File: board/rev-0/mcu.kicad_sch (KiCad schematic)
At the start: 53 parts, among them J1 I2C, J2 Conn_01x08, J3 USB_C_Receptacle_USB2.0_16P, J4 Conn_01x03, J5 Conn_01x03, J6 Conn_01x03, J7 Conn_01x03, U1 ESP32-S3-WROOM-1, U7 SN74LV1T34DBV

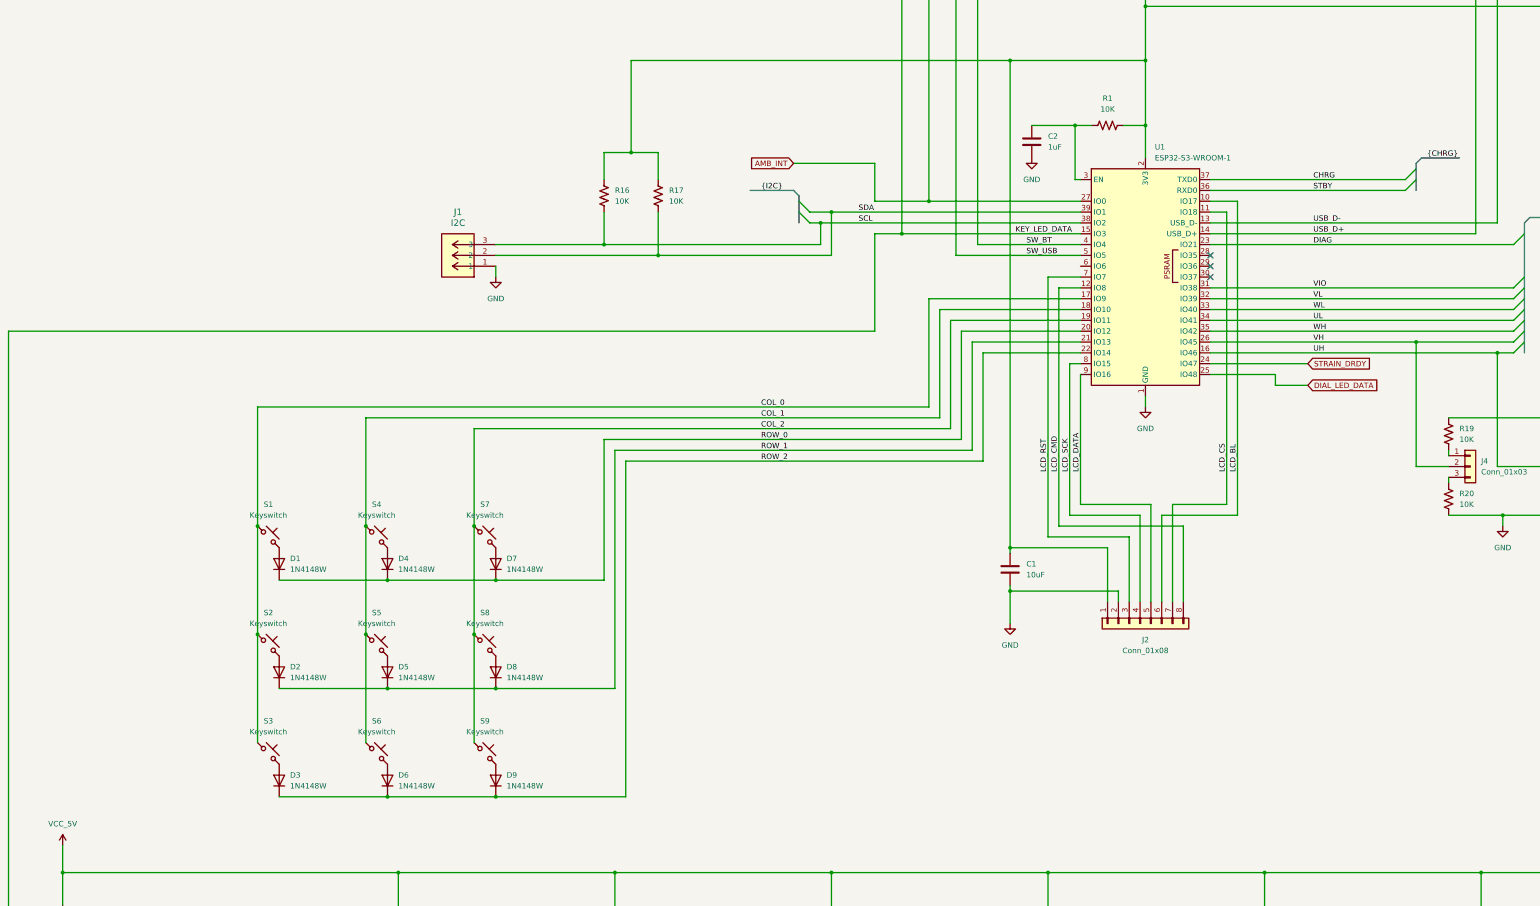
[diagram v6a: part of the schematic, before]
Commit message: Added power circuitry
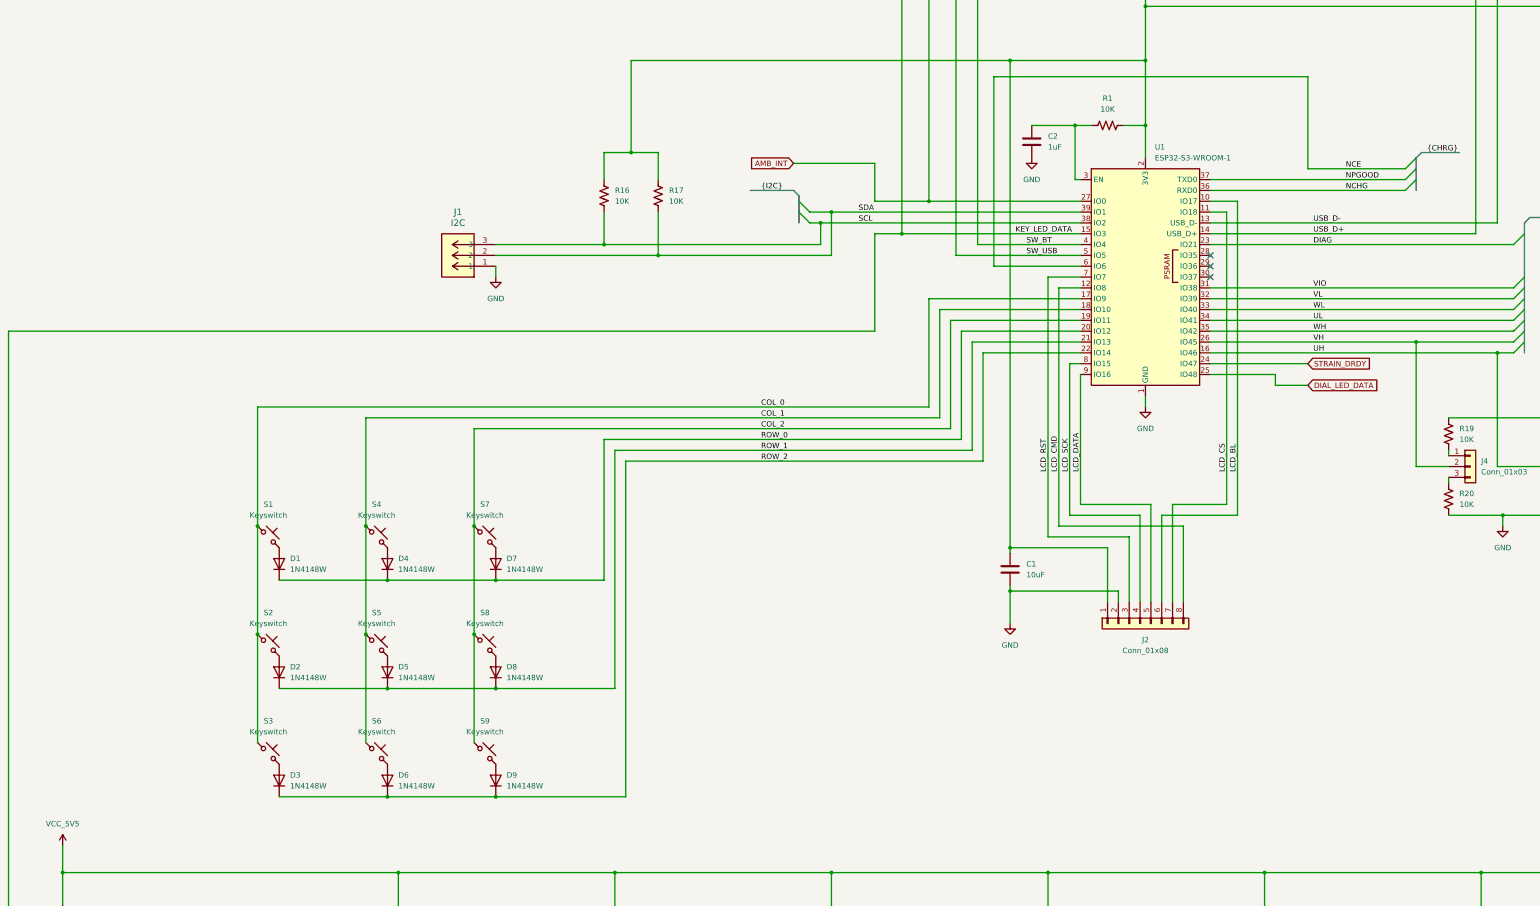
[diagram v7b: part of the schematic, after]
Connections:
- net NCE: now reaches U1.6 (IO6)
- net CHRG renamed NPGOOD
- net STBY renamed NCHG
- net VCC_5V renamed VCC_5V5
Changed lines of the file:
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@@
 	(title_block
 		(title "MCU")
-		(date "2025-03-28")
+		(date "2025-04-20")
 		(rev "0")
 		(company "Biro")
@@
 	)
 	(bus_alias "CHRG"
-		(members "CHRG" "STBY")
+		(members "NPGOOD" "NCHG" "NCE")
 	)
 	(junction
@@
 	)
 	(bus_entry
+		(at 368.3 177.8)
+		(size -2.54 2.54)
+		(stroke
+			(width 0)
+			(type default)
+		)
+	)
+	(bus_entry
 		(at 223.52 185.42)
 		(size 2.54 2.54)
@@
 	)
 	(bus_entry
-		(at 368.3 177.8)
+		(at 393.7 213.36)
 		(size -2.54 2.54)
 		(stroke
@@
 	)
 	(bus_entry
-		(at 393.7 213.36)
+		(at 368.3 175.26)
 		(size -2.54 2.54)
 		(stroke
@@
 	(wire
 		(pts
+			(xy 342.9 156.21) (xy 269.24 156.21)
+		)
+		(stroke
+			(width 0)
+			(type default)
+		)
+	)
+	(wire
+		(pts
 			(xy 311.15 256.54) (xy 311.15 279.4)
 		)
@@
 		)
 	)
+	(bus
+		(pts
+			(xy 368.3 177.8) (xy 368.3 175.26)
+		)
+		(stroke
+			(width 0)
+			(type default)
+		)
+	)
 	(wire
 		(pts
@@
 		)
 	)
-	(bus
-		(pts
-			(xy 368.3 176.53) (xy 368.3 177.8)
-		)
-		(stroke
-			(width 0)
-			(type default)
-		)
-	)
 	(wire
 		(pts
@@
 		)
 	)
+	(wire
+		(pts
+			(xy 365.76 177.8) (xy 342.9 177.8)
+		)
+		(stroke
+			(width 0)
+			(type default)
+		)
+	)
 	(bus
 		(pts
@@
 	(wire
 		(pts
-			(xy 320.04 182.88) (xy 365.76 182.88)
-		)
-		(stroke
-			(width 0)
-			(type default)
-		)
-	)
-	(wire
-		(pts
 			(xy 320.04 205.74) (xy 391.16 205.74)
 		)
@@
 		)
 	)
-	(bus
-		(pts
-			(xy 369.57 175.26) (xy 378.46 175.26)
-		)
-		(stroke
-			(width 0)
-			(type default)
-		)
-	)
 	(wire
 		(pts
@@
 		)
 	)
-	(wire
+	(bus
 		(pts
-			(xy 320.04 180.34) (xy 365.76 180.34)
+			(xy 369.57 173.99) (xy 378.46 173.99)
 		)
 		(stroke
@@
 	(wire
 		(pts
+			(xy 342.9 177.8) (xy 342.9 156.21)
+		)
+		(stroke
+			(width 0)
+			(type default)
+		)
+	)
+	(wire
+		(pts
 			(xy 231.14 342.9) (xy 231.14 358.14)
 		)
@@
 		)
 	)
+	(bus
+		(pts
+			(xy 368.3 182.88) (xy 368.3 180.34)
+		)
+		(stroke
+			(width 0)
+			(type default)
+		)
+	)
 	(wire
 		(pts
@@
 		)
 	)
-	(bus
+	(wire
 		(pts
-			(xy 393.7 205.74) (xy 393.7 208.28)
+			(xy 269.24 156.21) (xy 269.24 200.66)
 		)
 		(stroke
@@
 		)
 	)
-	(wire
+	(bus
 		(pts
-			(xy 262.89 92.71) (xy 270.51 92.71)
+			(xy 393.7 205.74) (xy 393.7 208.28)
 		)
 		(stroke
@@
 	(wire
 		(pts
-			(xy 186.69 114.3) (xy 186.69 99.06)
+			(xy 262.89 92.71) (xy 270.51 92.71)
 		)
 		(stroke
@@
 	(wire
 		(pts
-			(xy 332.74 342.9) (xy 332.74 358.14)
+			(xy 186.69 114.3) (xy 186.69 99.06)
 		)
 		(stroke
@@
 		)
 	)
-	(wire
+	(bus
 		(pts
-			(xy 535.94 342.9) (xy 535.94 358.14)
+			(xy 368.3 180.34) (xy 368.3 177.8)
 		)
 		(stroke
@@
 	(wire
 		(pts
-			(xy 485.14 365.76) (xy 490.22 365.76)
+			(xy 332.74 342.9) (xy 332.74 358.14)
 		)
 		(stroke
@@
 	(wire
 		(pts
-			(xy 289.56 180.34) (xy 288.29 180.34)
+			(xy 535.94 342.9) (xy 535.94 358.14)
 		)
 		(stroke
@@
 		)
 	)
-	(bus
+	(wire
 		(pts
-			(xy 368.3 177.8) (xy 368.3 180.34)
+			(xy 485.14 365.76) (xy 490.22 365.76)
 		)
 		(stroke
@@
 		)
 	)
-	(bus
+	(wire
 		(pts
-			(xy 368.3 180.34) (xy 368.3 182.88)
+			(xy 289.56 180.34) (xy 288.29 180.34)
 		)
 		(stroke
@@
 	(wire
 		(pts
+			(xy 320.04 182.88) (xy 365.76 182.88)
+		)
+		(stroke
+			(width 0)
+			(type default)
+		)
+	)
+	(wire
+		(pts
 			(xy 127 325.12) (xy 152.4 325.12)
 		)
@@
 		)
 	)
-	(bus
-		(pts
-			(xy 368.3 176.53) (xy 369.57 175.26)
-		)
-		(stroke
-			(width 0)
-			(type default)
-		)
-	)
 	(wire
 		(pts
@@
 	(wire
 		(pts
+			(xy 320.04 180.34) (xy 365.76 180.34)
+		)
+		(stroke
+			(width 0)
+			(type default)
+		)
+	)
+	(bus
+		(pts
+			(xy 368.3 175.26) (xy 369.57 173.99)
+		)
+		(stroke
+			(width 0)
+			(type default)
+		)
+	)
+	(wire
+		(pts
 			(xy 215.9 110.49) (xy 215.9 111.76)
 		)
@@
 	(wire
 		(pts
+			(xy 269.24 200.66) (xy 289.56 200.66)
+		)
+		(stroke
+			(width 0)
+			(type default)
+		)
+	)
+	(wire
+		(pts
 			(xy 382.27 193.04) (xy 320.04 193.04)
 		)
@@
 		)
 	)
+	(label "NCHG"
+		(at 351.79 182.88 0)
+		(effects
+			(font
+				(size 1.27 1.27)
+			)
+			(justify left bottom)
+		)
+	)
 	(label "USB_D-"
 		(at 344.17 190.5 0)
@@
 		)
 	)
+	(label "NCE"
+		(at 351.79 177.8 0)
+		(effects
+			(font
+				(size 1.27 1.27)
+			)
+			(justify left bottom)
+		)
+	)
 	(label "VH"
 		(at 344.17 218.44 0)
@@
 		)
 	)
-	(label "CHRG"
-		(at 344.17 180.34 0)
-		(effects
-			(font
-				(size 1.27 1.27)
-			)
-			(justify left bottom)
-		)
-	)
 	(label "DIAG"
 		(at 344.17 195.58 0)
@@
 		)
 	)
-	(label "STBY"
-		(at 344.17 182.88 0)
-		(effects
-			(font
-				(size 1.27 1.27)
-			)
-			(justify left bottom)
-		)
-	)
 	(label "VL"
 		(at 344.17 208.28 0)
@@
 		)
 	)
+	(label "{CHRG}"
+		(at 370.84 173.99 0)
+		(effects
+			(font
+				(size 1.27 1.27)
+			)
+			(justify left bottom)
+		)
+	)
 	(label "UH"
 		(at 344.17 220.98 0)
@@
 		)
 	)
-	(label "LCD_DATA"
-		(at 289.56 248.92 90)
+	(label "NPGOOD"
+		(at 351.79 180.34 0)
 		(effects
 			(font
@@
 		)
 	)
-	(label "{CHRG}"
-		(at 370.84 175.26 0)
+	(label "LCD_DATA"
+		(at 289.56 248.92 90)
 		(effects
 			(font
@@
 			)
 		)
-		(property "Value" "VCC_5V"
+		(property "Value" "VCC_5V5"
 			(at 50.8 331.47 0)
 			(effects
@@
 			)
 		)
-		(property "Description" "Power symbol creates a global label with name \"VCC_5V\""
+		(property "Description" "Power symbol creates a global label with name \"VCC_5V5\""
 			(at 50.8 336.55 0)
 			(effects

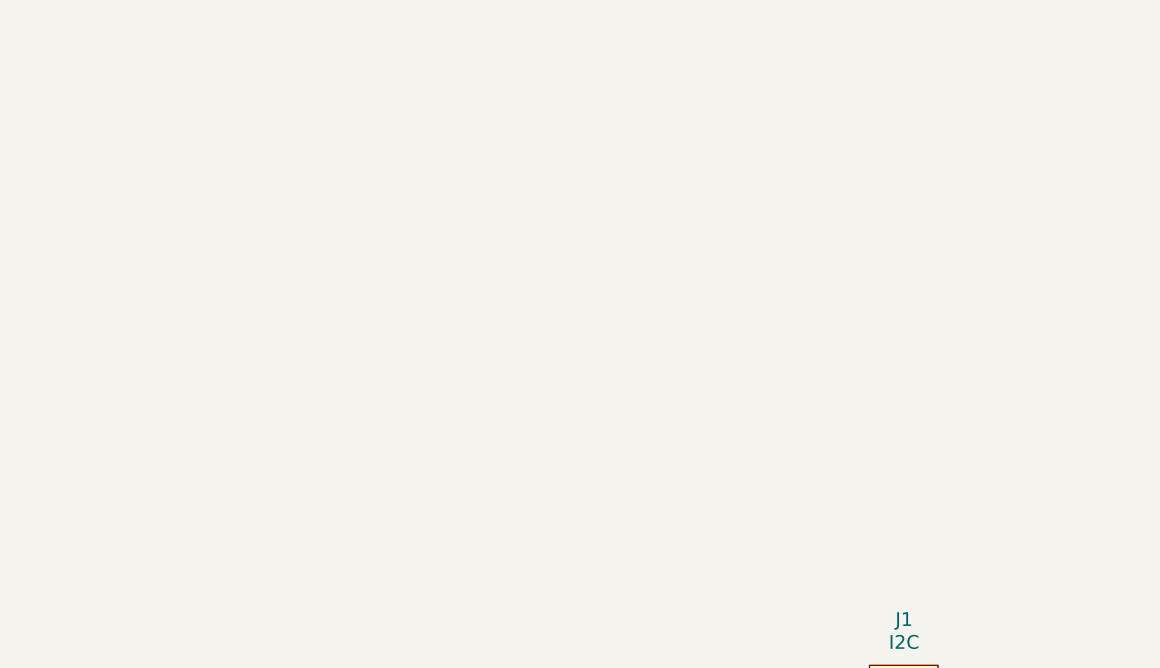
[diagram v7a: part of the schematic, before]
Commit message: First crack at layout, added scottokeebs 3d files
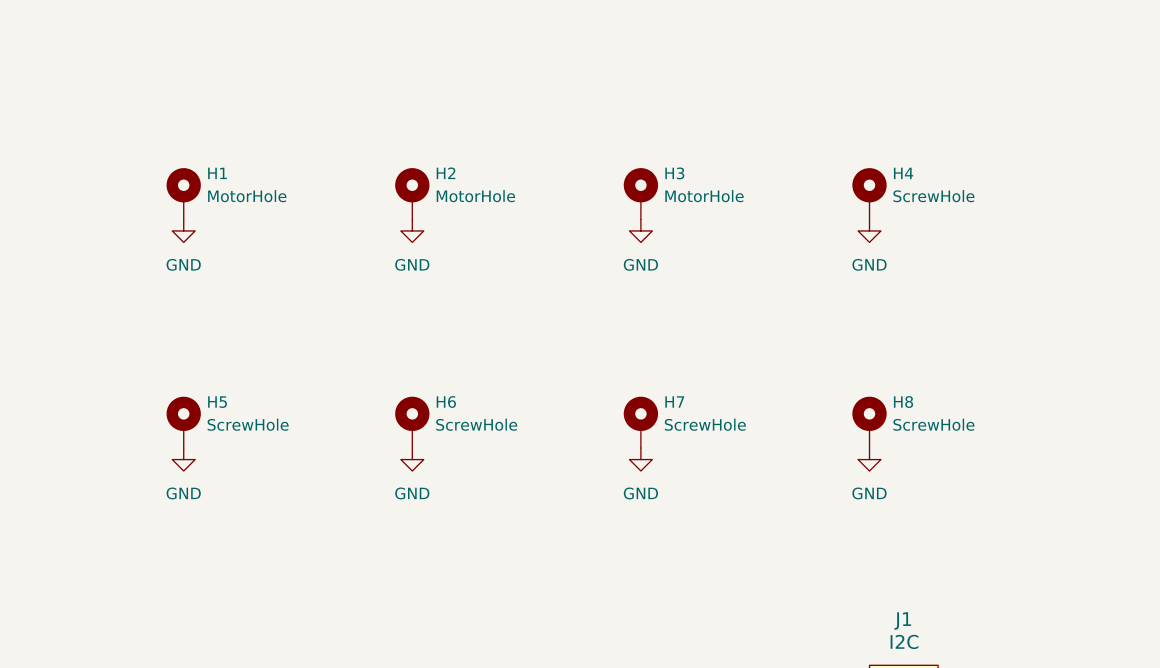
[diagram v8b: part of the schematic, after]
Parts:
- added H1, H2, H3: MotorHole, Holes:MountingHole_M1.6, symbol Mechanical:MountingHole_Pad
- added H4, H5, H6, H7, H8: ScrewHole, MountingHole:MountingHole_2.2mm_M2_ISO7380_Pad, symbol Mechanical:MountingHole_Pad
- C1, C2: footprint (none) -> Capacitor_SMD:C_0603_1608Metric
- J4, J5, J6, J7: footprint (none) -> Connector_PinHeader_2.54mm:PinHeader_1x03_P2.54mm_Vertical
- R1, R16, R17, R18, R19, R2, R20, R21, R22, R23, R24, R25, R26, R3: footprint (none) -> Resistor_SMD:R_0603_1608Metric
- S1, S2, S3, S4, S5, S6, S7, S8, S9: footprint (none) -> ScottoKeebs_MX:MX_PCB_1.00u
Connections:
- net GND: now also H1.1, H2.1, H3.1, H4.1, H5.1, H6.1, H7.1, H8.1
